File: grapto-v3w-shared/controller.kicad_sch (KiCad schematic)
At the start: 31 parts, among them J5 Conn_01x06_Female, J6 USB_C_Receptacle_USB2.0, J7 USB_C_Receptacle_USB2.0, J8 Conn_01x06_Male, U11 USBLC6-4SC6, U13 TPS2110, U14 LM3676SD-3.3, U16 Laird_bl653

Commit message: update generated pcbs
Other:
- added sheet matrix (../grapto-v3w-shared/matrix.kicad_sch)
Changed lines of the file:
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@@
     (pin "2")
+  )
+  (sheet (at 19.685 75.565) (size 31.75 34.29) (fields_autoplaced)
+    (stroke (width 0.1524) (type solid) (color 0 0 0 0))
+    (fill (color 0 0 0 0.0000))
+    (property "Sheet name" "matrix" (id 0) (at 19.685 74.8534 0)
+      (effects (font (size 1.27 1.27)) (justify left bottom))
+    )
+    (property "Sheet file" "../grapto-v3w-shared/matrix.kicad_sch" (id 1) (at 19.685 110.4396 0)
+      (effects (font (size 1.27 1.27)) (justify left top))
+    )
   )
   (sheet (at 44.45 25.4) (size 23.495 22.86) (fields_autoplaced)

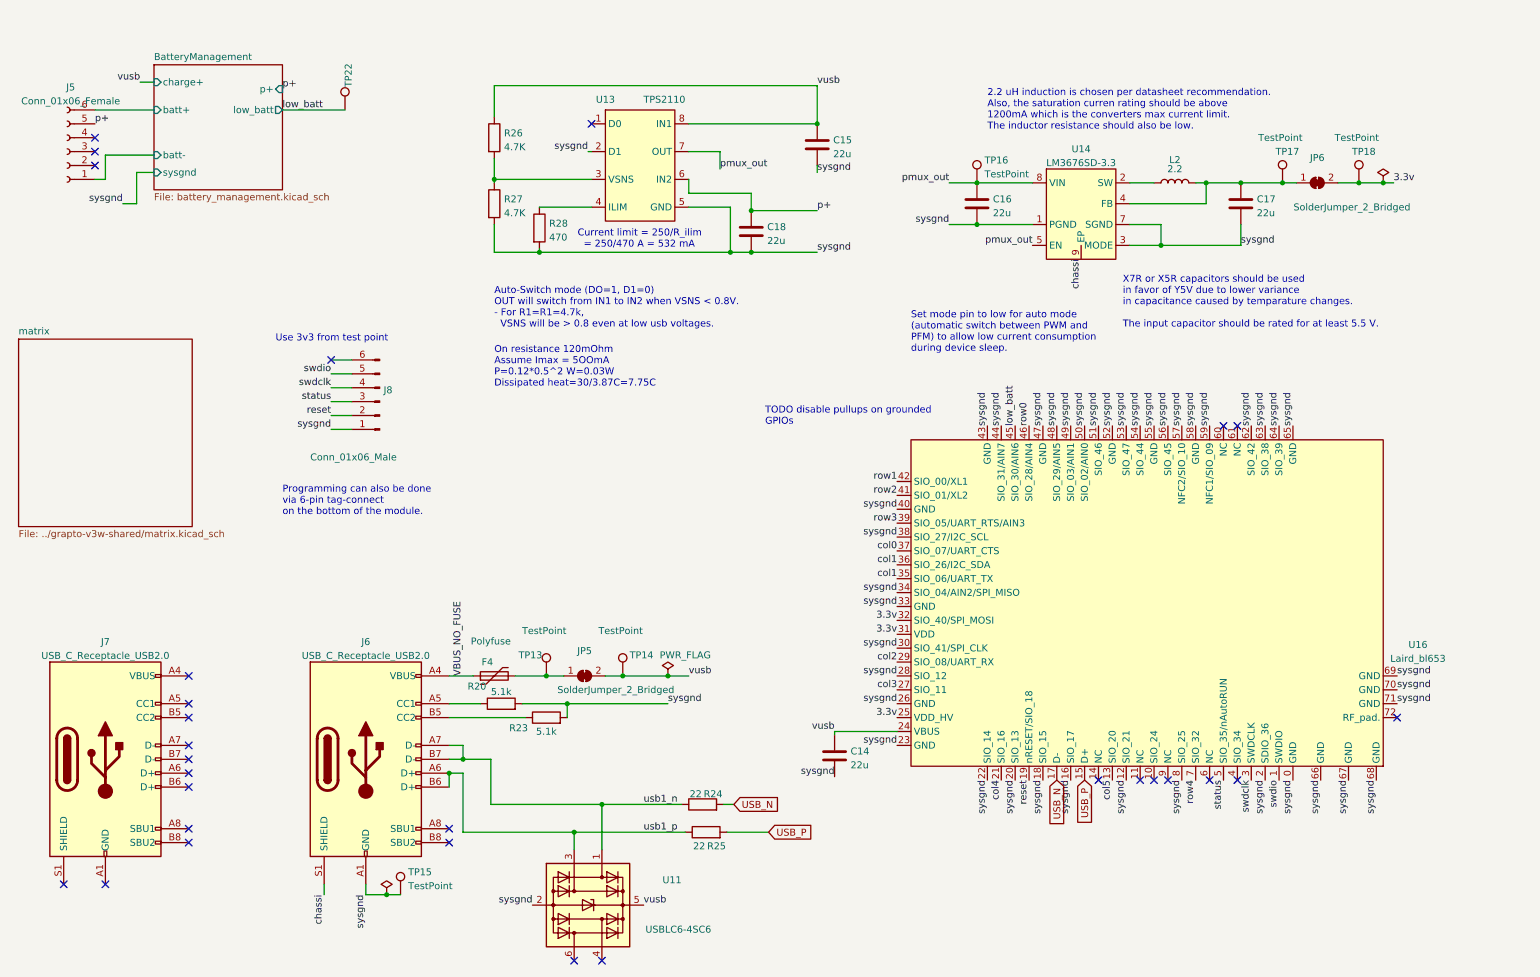
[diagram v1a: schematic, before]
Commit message: Redesign pcb with new mcu and charger
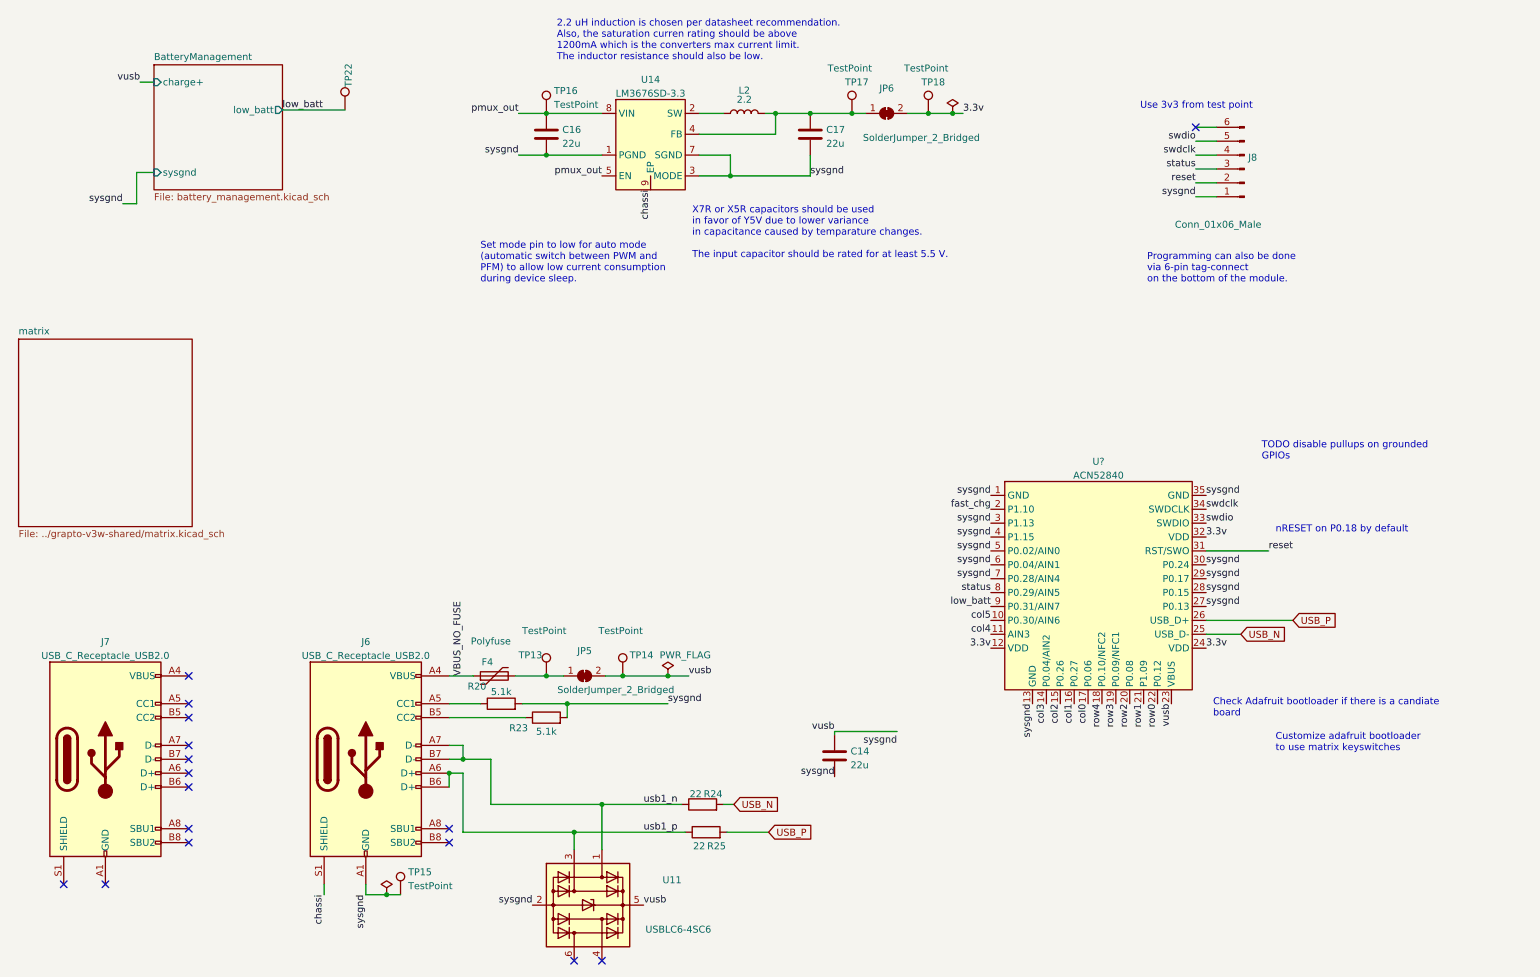
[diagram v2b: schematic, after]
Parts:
- removed C15, C18: 22u, Fuse:Fuse_0603_1608Metric_Pad1.05x0.95mm_HandSolder, symbol Device:C
- removed J5: Conn_01x06_Female, grapto-v3w:df65-6P-1.7V, symbol Connector:Conn_01x06_Female
- removed R26, R27: 4.7K, Resistor_SMD:R_0603_1608Metric_Pad0.98x0.95mm_HandSolder, symbol Device:R
- removed R28: 470, Resistor_SMD:R_0603_1608Metric_Pad0.98x0.95mm_HandSolder, symbol Device:R
- removed U13: TPS2110, Package_SO:TSSOP-8_4.4x3mm_P0.65mm, symbol grapto-v3w:TPS2110
- removed U16: Laird_bl653, grapto-v3w:Laird_bl653, symbol grapto-v3w:Laird_bl653
- added U?: ACN52840, symbol grapto-v3w:ACN52840
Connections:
- net 3.3v: now also U?.12 (VDD), U?.24 (VDD), U?.32 (VDD)
- net USB_N: now also U?.25 (USB_D-)
- net USB_P: now also U?.26 (USB_D+)
- net col0: now also U?.17 (P0.06)
- net col1: now also U?.16 (P0.27)
- net col2: now also U?.15 (P0.26)
- net col3: now also U?.14 (P0.04/AIN2)
- net col4: now also U?.11 (AIN3)
- net col5: now also U?.10 (P0.30/AIN6)
- net low_batt: now also U?.9 (P0.31/AIN7)
- net reset: now also U?.31 (RST/SWO)
- net row0: now also U?.22 (P0.12)
- net row1: now also U?.21 (P1.09)
- net row2: now also U?.20 (P0.08)
- net row3: now also U?.19 (P0.09/NFC1)
- net row4: now also U?.18 (P0.10/NFC2)
- net status: now also U?.8 (P0.29/AIN5)
- net swdclk: now also U?.34 (SWDCLK)
- net swdio: now also U?.33 (SWDIO)
- net sysgnd: now also U?.1 (GND), U?.13 (GND), U?.27 (P0.13), U?.28 (P0.15), U?.29 (P0.17), U?.3 (P1.13), U?.30 (P0.24), U?.35 (GND), U?.4 (P1.15), U?.5 (P0.02/AIN0), U?.6 (P0.04/AIN1), U?.7 (P0.28/AIN4)
- net vusb: now also U?.23 (VBUS)
- new net fast_chg: U?.2 (P1.10)
- no-connect marks 29 -> 16
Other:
- sheet BatteryManagement ports: added none; removed batt+, batt-, p+
- note added: "Check Adafruit bootloader if there is a candiate board"
- note added: "Customize adafruit bootloader to use matrix keyswitches"
- note added: "nRESET on P0.18 by default"
- note removed: "Auto-Switch mode (DO=1, D1=0) OUT will switch from IN1 to IN2 when VSNS < 0.8V. - For R1=R1=4.7k, VSNS will be > 0.8 even at low usb voltages."
- note removed: "Current limit = 250/R_ilim = 250/470 A = 532 mA"
- note removed: "On resistance 120mOhm Assume Imax = 5OOmA P=0.12*0.5^2 W=0.03W Dissipated heat=30/3.87C=7.75C"
- moved on the sheet: C16, C17, J8, JP6, L2, TP16, TP17, TP18, U14

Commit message: schematic rewrite draft done.
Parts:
- removed J7: USB_C_Receptacle_USB2.0, grapto-v3w:USB_C_Receptacle_molex_2169900001, symbol Connector:USB_C_Receptacle_USB2.0
- added D30: LED, LED_SMD:LED_0805_2012Metric_Pad1.15x1.40mm_HandSolder, symbol Device:LED
- added J1: Conn_01x02_Female, Connector_JST:JST_PH_S2B-PH-SM4-TB_1x02-1MP_P2.00mm_Horizontal, symbol Connector:Conn_01x02_Female
- added R1: 5.6, Resistor_SMD:R_0603_1608Metric_Pad0.98x0.95mm_HandSolder, symbol Device:R
- U1: renamed from U?; footprint (none) -> grapto-v3w:ACN52840
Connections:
- net 3.3v: now also J8.6 (Pin_6)
- net status: now also R1.1
- net sysgnd: now also D30.1 (K), J1.1 (Pin_1)
- net cc1: now reaches J6.A5 (CC1), R20.1
- net cc2: now reaches J6.B5 (CC2), R23.1
- net VBUS_NO_FUSE renamed vbus_no_fuse
- net pmux_out renamed vsys
- new net: D30.2 (A), R1.2
- new net BatteryManagement/bat+: J1.2 (Pin_2)
- no-connect marks 16 -> 4
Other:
- sheet BatteryManagement ports: added bat+, bat_level, fast_chg, vsys, vusb; removed charge+, low_batt
- note added: "Customize adafruit bootloader to use matrix keyswitches for DFU and FRST"
- note added: "I_led = 20 mA V_led = 3.25 V R_led = (V - V_led)/I_led R_blue = (3.3 - 3.2)/0.02 = 5 ohm"
- note removed: "Check Adafruit bootloader if there is a candiate board"
- note removed: "Customize adafruit bootloader to use matrix keyswitches"
- moved on the sheet: TP22

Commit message: Schematic work.
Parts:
- removed C14: 22u, Fuse:Fuse_0603_1608Metric_Pad1.05x0.95mm_HandSolder, symbol Device:C
- removed U11: USBLC6-4SC6, Package_TO_SOT_SMD:SOT-23-6, symbol Power_Protection:USBLC6-4SC6
- removed U14: LM3676SD-3.3, Package_SON:WSON-8-1EP_3x3mm_P0.5mm_EP1.6x2.0mm, symbol grapto-v3w:LM3676SD-3.3
- added C?: 120p, Fuse:Fuse_0603_1608Metric_Pad1.05x0.95mm_HandSolder, symbol Device:C
- added R?: 400k, symbol Device:R
- added R?: 100k, symbol Device:R
- added SW?: SW_Push, symbol Switch:SW_Push
- added U?: USBLC6-2SC6, Package_TO_SOT_SMD:SOT-23-6, symbol Power_Protection:USBLC6-2SC6
- added U?: TPS62822DLC, Package_DFN_QFN:Texas_VSON-HR-8_1.5x2mm_P0.5mm, symbol Regulator_Switching:TPS62822DLC
- L2: value 2.2 -> 470n
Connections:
- net 3.3v: no longer JP6.2 (B), TP18.1, U1.12 (VDD), U1.24 (VDD), U1.32 (VDD)
- net reset: now also SW?.1
- net sysgnd: now also R?.2, SW?.2, U?.2 (GND), U?.3 (AGND), U?.5 (PGND)
- net usb1_n: now also U?.1 (I/O1), U?.6 (I/O1)
- net usb1_p: now also U?.3 (I/O2), U?.4 (I/O2)
- net vsys: now also U?.1 (EN), U?.7 (VIN)
- net vusb: now also U?.5 (VBUS)
- net at C17.1, JP6.1 (A), L2.2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: now also C?.1, R?.1
- net at L2.1: now also U?.6 (SW)
- new net: C?.2, R?.1, R?.2, U?.2 (FB)
- new net 3.0V: JP6.2 (B), TP18.1, U1.12 (VDD), U1.24 (VDD), U1.32 (VDD)
- no-connect marks 4 -> 3
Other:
- note added: "10 uH induction is chosen per datasheet recommendation. Also, the saturation curren rating should be above max expected inductor current: I_lmax = Ioutmax + deltaI_L/2 = = Ioutmax + V_out*(1-Vout/Vin)/(2*L*f) = 3.3*(1-3.3/4.4)/(10*650*2)+300 ~ 300 Also the DC resistance should be low"
- note added: "X7R or X5R capacitors should be used in favor of Y5V due to lower variance in capacitance caused by temparature changes. The input capacitor should be rated for at least 4.4 V."
- note added: "r1=r2*(Vout/0.6-1)=r2*(3/0.6-1)=4 R2 should be less than 120kOhm per datasheet recommendation."
- note removed: "2.2 uH induction is chosen per datasheet recommendation. Also, the saturation curren rating should be above 1200mA which is the converters max current limit. The inductor resistance should also be low."
- note removed: "Set mode pin to low for auto mode (automatic switch between PWM and PFM) to allow low current consumption during device sleep."
- note removed: "X7R or X5R capacitors should be used in favor of Y5V due to lower variance in capacitance caused by temparature changes. The input capacitor should be rated for at least 5.5 V."
- moved on the sheet: C17, JP6, R23, R24, R25, TP17, TP18

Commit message: Schematic fine-tuning.
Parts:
- removed JP5, JP6: SolderJumper_2_Bridged, Jumper:SolderJumper-2_P1.3mm_Bridged_RoundedPad1.0x1.5mm, symbol Jumper:SolderJumper_2_Bridged
- added C? (x4): 22u, Fuse:Fuse_0603_1608Metric_Pad1.05x0.95mm_HandSolder, symbol Device:C
- added D? (x2): LED, LED_SMD:LED_0805_2012Metric_Pad1.15x1.40mm_HandSolder, symbol Device:LED
- added R? (x3): 60, Resistor_SMD:R_0603_1608Metric_Pad0.98x0.95mm_HandSolder, symbol Device:R
- added R? (x2): 0.01m, symbol Device:R
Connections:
- net 3.3v is gone; now on net 3.0V: J8.6 (Pin_6)
- net 3.0V: now also C?.1, C?.1, C?.1, R?.2
- net sysgnd: now also C?.2, C?.2, C?.2, C?.2, D?.1 (K), D?.1 (K); no longer U1.3 (P1.13), U1.4 (P1.15)
- net vusb: now also C?.1, R?.2
- net at C17.1, C?.1, L2.2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: now also R?.1
- net at F4.2, TP13.1: now also R?.1
- new net: D?.2 (A), R?.2 (x2)
- new net: R?.1, R?.2
- new net bat_lvl1: R?.1, U1.3 (P1.13)
- new net bat_lvl2: R?.1, U1.4 (P1.15)
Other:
- note added: "I_led = 20 mA V_led = 3.25 V R_led = (V - V_led)/I_led R_green = (4.4 - 3.2)/0.02 = 60 ohm R_blue = (3.3 - 3.2)/0.02 = 5 ohm R_red = (4.4 - 2)/0.02 = 120 ohm"
- note added: "Led signals - charging, green == on - fast charging, blue == on - battery - high: green - mid: green+red - low: red - status, blue"
- note removed: "I_led = 20 mA V_led = 3.25 V R_led = (V - V_led)/I_led R_blue = (3.3 - 3.2)/0.02 = 5 ohm"
- moved on the sheet: D30, F4, J6, R1, R20, R23, R24, R25, SW?, TP13, TP14, TP15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
